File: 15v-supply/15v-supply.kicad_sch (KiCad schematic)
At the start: 25 parts, among them J1 15 VDC REGULATED, J2 Common, J3 -15 VDC REGULATED, T1 30VCT SEC, U1 L7815, U2 L7915

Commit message: changed schematic sheet notes
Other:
- company: Brandywine Valley Radio Company -> Andy McCann KA3KAF and Doug McCann KA3KAG
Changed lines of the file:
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@@
     (date "2022-06-05")
     (rev "0.0")
-    (company "Brandywine Valley Radio Company")
+    (company "Andy McCann KA3KAF and Doug McCann KA3KAG")
+    (comment 2 "Audiophile's Project Source Book, Fig 7-8")
+    (comment 3 "G. Randy Slone")
+    (comment 4 "Orginal Design by:")
   )
   (junction (at 143.51 127) (diameter 0) (color 0 0 0 0)

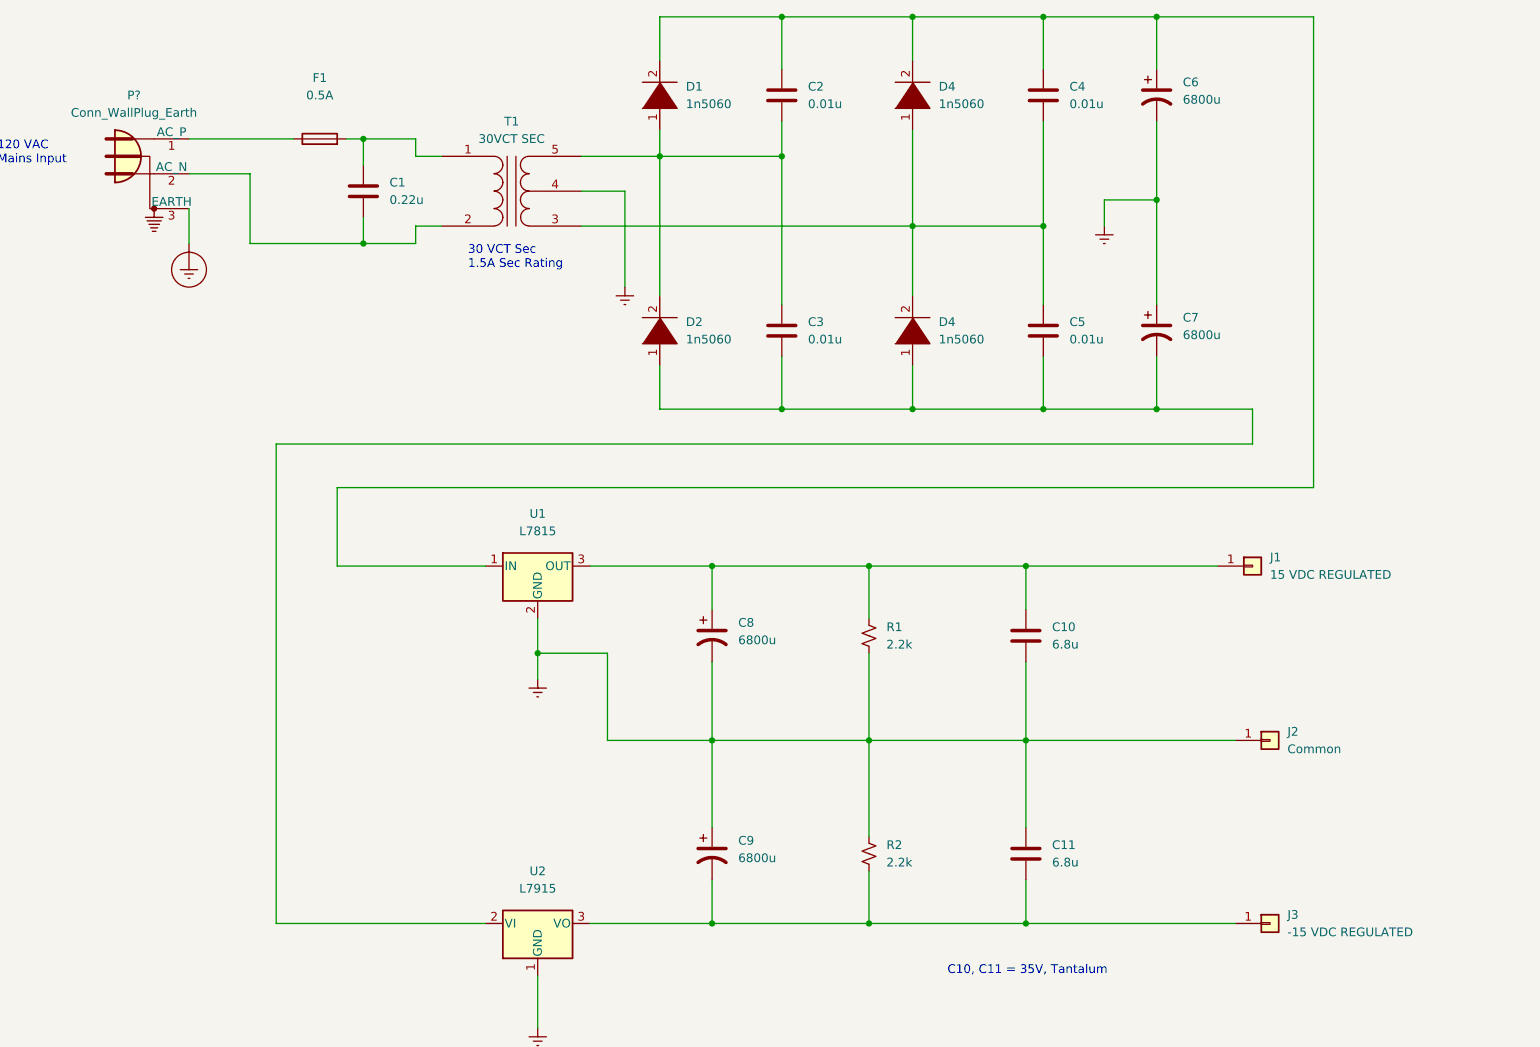
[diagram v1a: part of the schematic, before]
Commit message: added power flags, ERC checks pass
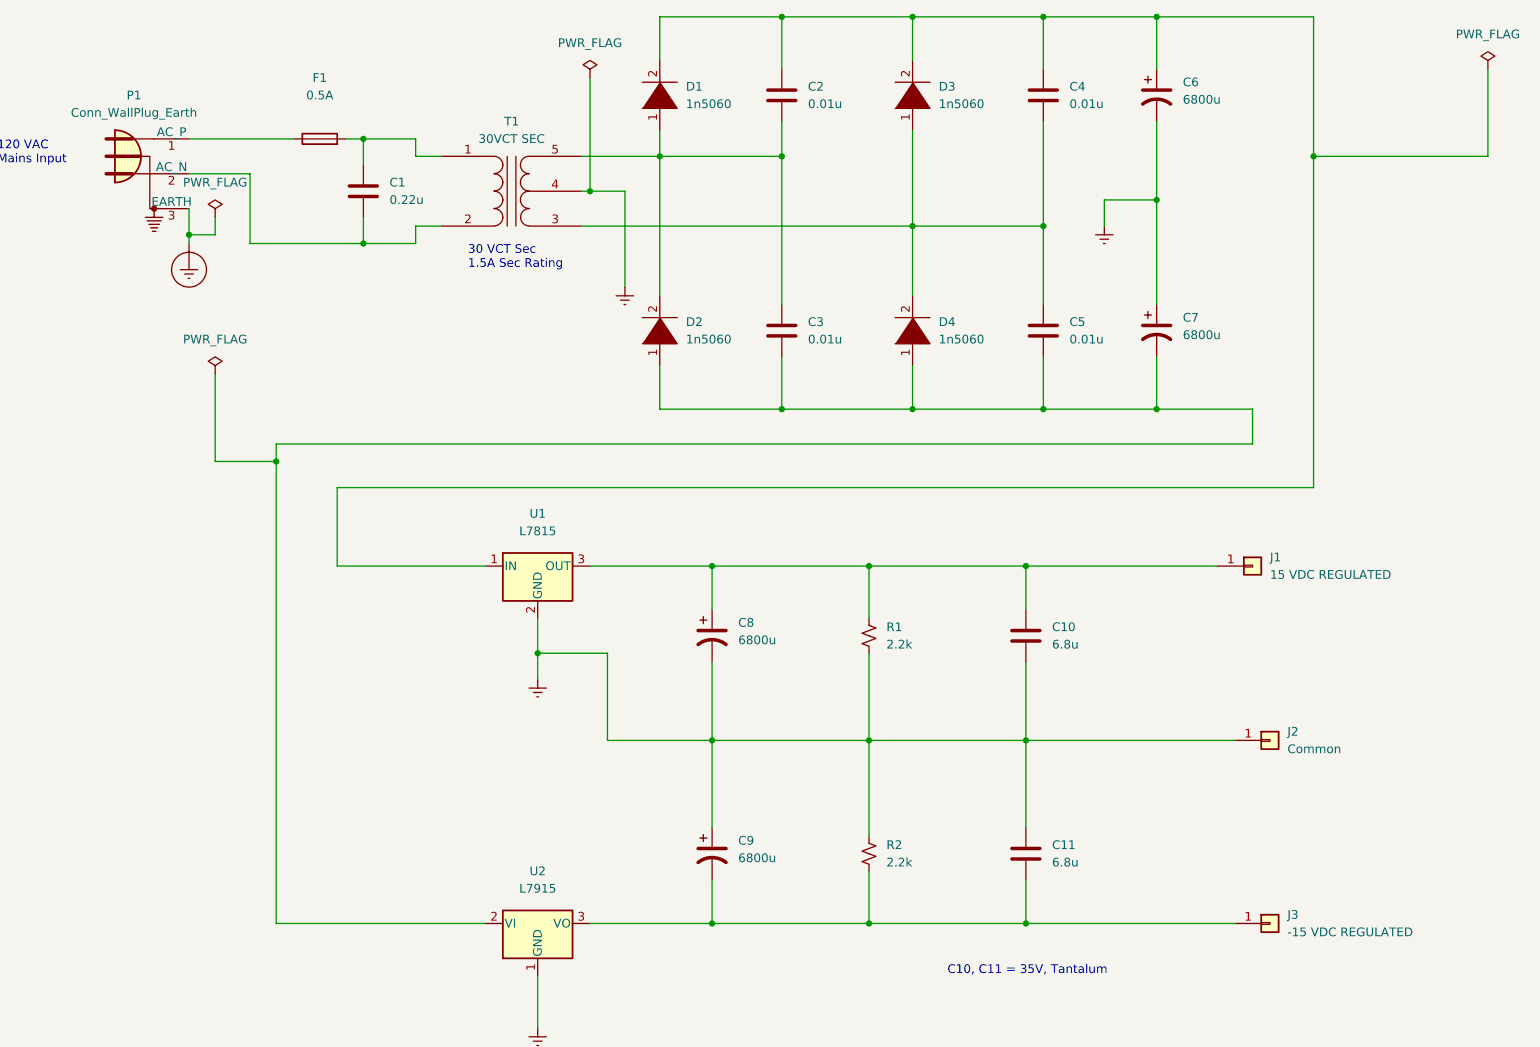
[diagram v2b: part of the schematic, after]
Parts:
- gave numbers to parts that had none: 1
- renumbered D4 to D3

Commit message: updated schematic -- cannot pass erc
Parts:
- removed J1: 15 VDC REGULATED, symbol Connector_Generic:Conn_01x01
- removed J2: Common, symbol Connector_Generic:Conn_01x01
- removed J3: -15 VDC REGULATED, symbol Connector_Generic:Conn_01x01
- removed T1: 30VCT SEC, symbol Device:Transformer_1P_SS
- added J1: Screw_Terminal_01x03, TerminalBlock_4Ucon:TerminalBlock_4Ucon_1x03_P3.50mm_Horizontal, symbol Connector:Screw_Terminal_01x03
- added T1: Transformer_1P_2S, symbol Device:Transformer_1P_2S
- C1: footprint (none) -> Capacitor_THT:C_Axial_L5.1mm_D3.1mm_P7.50mm_Horizontal
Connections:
- net Earth: now also J1.2 (Pin_2), T1.4 (SB), T1.5 (SC)
- net at C1.1, F1.2: now also T1.1 (AA)
- net at C1.2, P1.2 (AC_N): now also T1.2 (AB)
- net at C4.2, C5.1, D3.1 (K)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: now also T1.6 (SD)
- net at C2.2, C3.1, D1.1 (K)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: now also T1.3 (SA)
- net at C10.1, C8.1, R1.1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: now also J1.1 (Pin_1)
- net at C11.2, C9.2, R2.2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: now also J1.3 (Pin_3)
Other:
- note added: "-15V REGULATED"
- note added: "15V REGULATED"
- note added: "COMMON"
- note removed: "Source: Audiophile Project Sourcebook G. Randy Slone Fig 7-8"
- moved on the sheet: C1, C10, C11, C2, C3, C4, C5, C6, C7, C8, C9, D1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

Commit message: updates to 15 v supply and if log amp boards
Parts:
- C1, C10, C11, C2, C3, C4, C5: symbol Device:C -> Device:C_Small
- C6, C7, C8, C9: symbol Device:C_Polarized_US -> Device:C_Polarized_Small_US
- D1, D2, D3, D4: footprint (none) -> DO15-12; symbol pspice:DIODE -> 1N5060GP:1N5060GP; Spice_Lib_File (none) -> 1n5060.lib; Spice_Model (none) -> 1N5060; Spice_Netlist_Enabled (none) -> Y; Spice_Node_Sequence (none) -> 2 1; Spice_Primitive (none) -> D
- F1, J1: Spice_Netlist_Enabled (none) -> N; Spice_Primitive (none) -> R
- P1: value Conn_WallPlug_Earth -> 120VAC; Spice_Model (none) -> sin(0 169.7 60); Spice_Netlist_Enabled (none) -> Y; Spice_Primitive (none) -> V
- T1: value Transformer_1P_2S -> (none); Spice_Lib_File (none) -> xformer.lib; Spice_Model (none) -> XFORMER; Spice_Netlist_Enabled (none) -> Y; Spice_Primitive (none) -> X
- U1: Spice_Lib_File (none) -> regulators.lib; Spice_Model (none) -> LM7815; Spice_Netlist_Enabled (none) -> Y; Spice_Node_Sequence (none) -> 2 1 3; Spice_Primitive (none) -> X
- U2: Spice_Lib_File (none) -> regulators.lib; Spice_Model (none) -> LM7915; Spice_Netlist_Enabled (none) -> Y; Spice_Node_Sequence (none) -> 2 1 3; Spice_Primitive (none) -> X
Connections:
- net Earth_Protective is gone; now on net GND: P1.3 (EARTH)
- net at C2.1, C4.1, C6.1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: now also D1.C, D3.C; no longer D1.2 (A), D3.2 (A)
- net at C2.2, C3.1, T1.3 (SA): now also D1.A, D2.C; no longer D1.1 (K), D2.2 (A)
- net at C4.2, C5.1, T1.6 (SD): now also D3.A, D4.C; no longer D3.1 (K), D4.2 (A)
- net at C3.2, C5.2, C7.2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: now also D2.A, D4.A; no longer D2.1 (K), D4.1 (K)
- net Earth renamed GND
